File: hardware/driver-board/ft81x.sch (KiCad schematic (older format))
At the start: 4 parts, among them U4 FT813

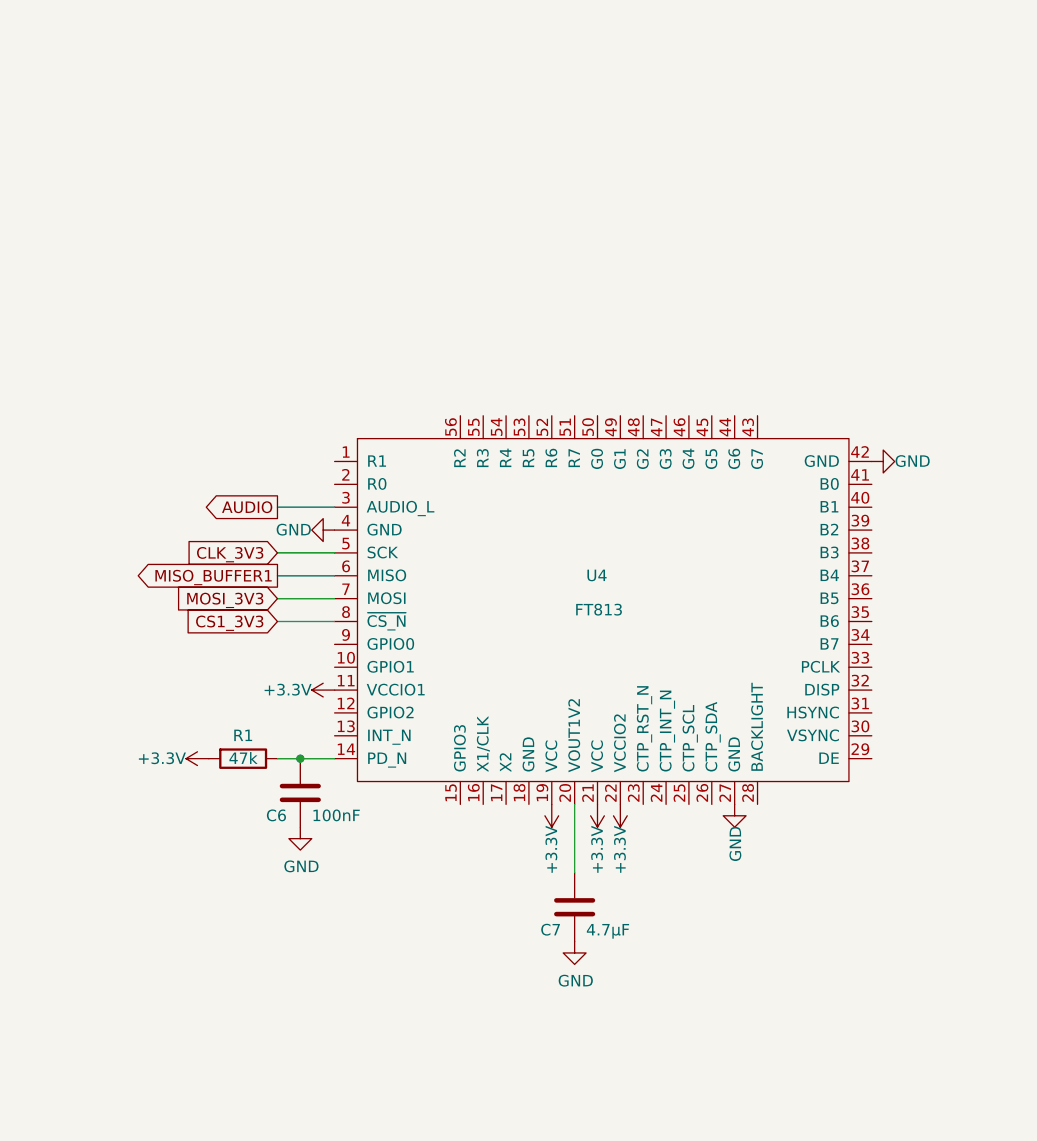
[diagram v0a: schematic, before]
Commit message: Rework power to four different voltage domains
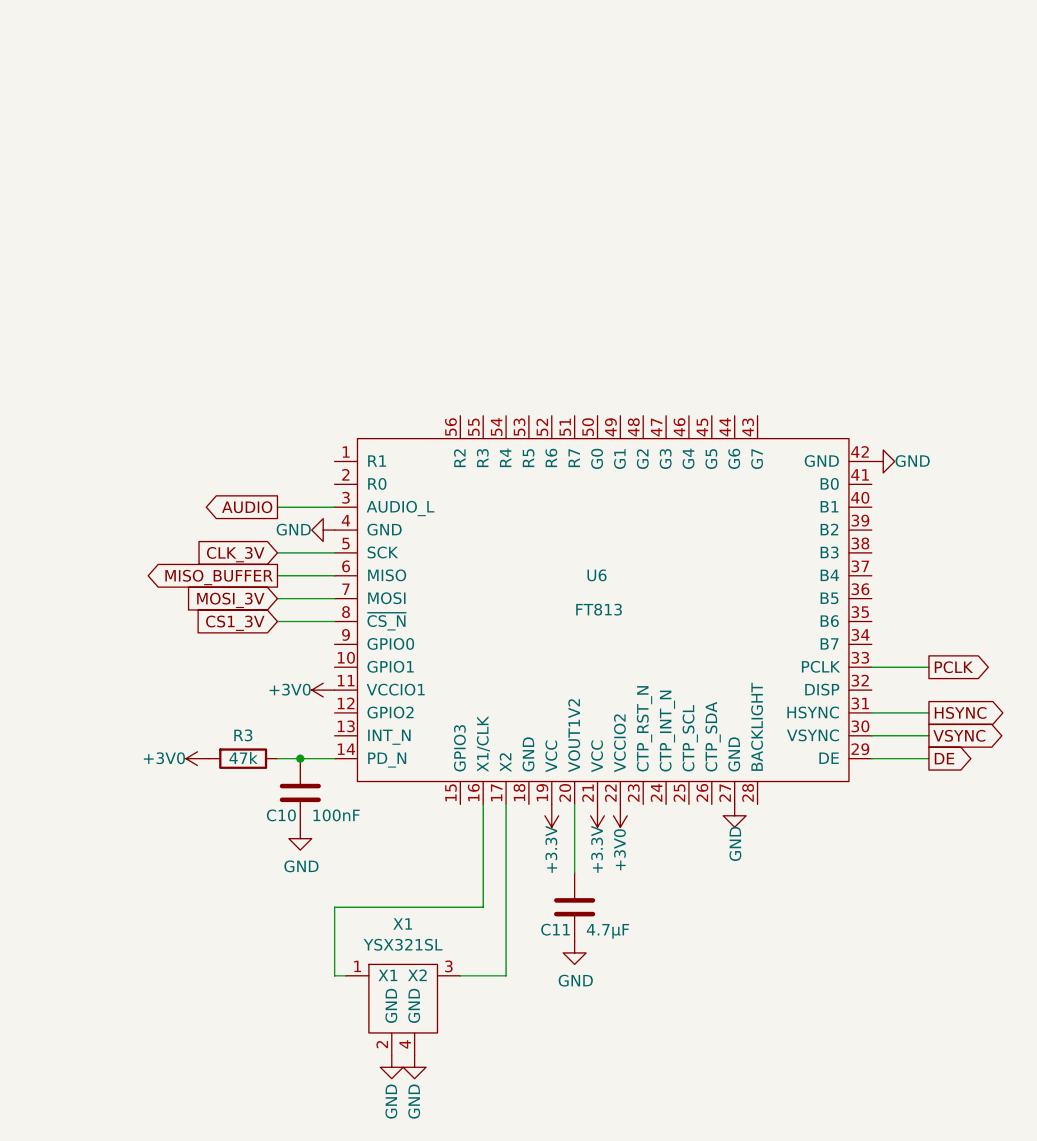
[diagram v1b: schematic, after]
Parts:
- added X1: YSX321SL, Crystal:Crystal_SMD_3225-4Pin_3.2x2.5mm, symbol driver-board:YSX321SL
- renumbered C6 to C10, C7 to C11, R1 to R3, U4 to U6
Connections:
- net +3V3: no longer R3.2, U6.11 (VCCIO1), U6.22 (VCCIO2)
- net GND: now also X1.2 (GND), X1.4 (GND)
- net at U6.16 (X1/CLK): now also X1.1 (X1)
- net at U6.17 (X2): now also X1.3 (X2)
- net DE: now reaches U6.29 (DE)
- net VSYNC: now reaches U6.30 (VSYNC)
- net HSYNC: now reaches U6.31 (HSYNC)
- net PCLK: now reaches U6.33 (PCLK)
- net CLK_3V3 renamed CLK_3V
- net CS1_3V3 renamed CS1_3V
- net MISO_BUFFER1 renamed MISO_BUFFER
- net MOSI_3V3 renamed MOSI_3V
- new net +3V0: R3.2, U6.11 (VCCIO1), U6.22 (VCCIO2)
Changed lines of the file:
@@
 $EndDescr
 $Comp
-L driver-board:FT813 U4
+L driver-board:FT813 U6
 U 1 1 5F0268C1
 P 5950 3750
-F 0 "U4" H 5900 3900 50  0000 L CNN
+F 0 "U6" H 5900 3900 50  0000 L CNN
 F 1 "FT813" H 5850 3750 50  0000 L CNN
 F 2 "Package_DFN_QFN:QFN-56-1EP_8x8mm_P0.5mm_EP5.6x5.6mm_HandSolder" H 5950 3750 50  0001 C CNN
@@
 AUDIO
 Text GLabel 4550 3500 0    50   Input ~ 0
-CLK_3V3
+CLK_3V
 Text GLabel 4550 3600 0    50   Output ~ 0
-MISO_BUFFER1
+MISO_BUFFER
 Text GLabel 4550 3700 0    50   Input ~ 0
-MOSI_3V3
+MOSI_3V
 Text GLabel 4550 3800 0    50   Input ~ 0
-CS1_3V3
-$Comp
-L power:GND #PWR021
+CS1_3V
+$Comp
+L power:GND #PWR034
 U 1 1 5F02B6C5
 P 4800 3400
-F 0 "#PWR021" H 4800 3150 50  0001 C CNN
+F 0 "#PWR034" H 4800 3150 50  0001 C CNN
 F 1 "GND" V 4800 3300 50  0000 R CNN
 F 2 "" H 4800 3400 50  0001 C CNN
@@
 $EndComp
 $Comp
-L power:+3.3V #PWR022
-U 1 1 5F02BA0F
-P 4800 4100
-F 0 "#PWR022" H 4800 3950 50  0001 C CNN
-F 1 "+3.3V" V 4800 4200 50  0000 L CNN
-F 2 "" H 4800 4100 50  0001 C CNN
-F 3 "" H 4800 4100 50  0001 C CNN
-	1    4800 4100
-	0    -1   -1   0
-$EndComp
-$Comp
-L power:+3.3V #PWR024
+L power:+3.3V #PWR037
 U 1 1 5F02BC5F
 P 5750 4600
-F 0 "#PWR024" H 5750 4450 50  0001 C CNN
+F 0 "#PWR037" H 5750 4450 50  0001 C CNN
 F 1 "+3.3V" V 5750 4800 50  0000 C CNN
 F 2 "" H 5750 4600 50  0001 C CNN
@@
 $EndComp
 $Comp
-L power:+3.3V #PWR025
+L power:+3.3V #PWR038
 U 1 1 5F02BEAA
 P 5950 4600
-F 0 "#PWR025" H 5950 4450 50  0001 C CNN
+F 0 "#PWR038" H 5950 4450 50  0001 C CNN
 F 1 "+3.3V" V 5950 4800 50  0000 C CNN
 F 2 "" H 5950 4600 50  0001 C CNN
@@
 $EndComp
 $Comp
-L power:+3.3V #PWR026
-U 1 1 5F02C0C1
-P 6050 4600
-F 0 "#PWR026" H 6050 4450 50  0001 C CNN
-F 1 "+3.3V" V 6050 4800 50  0000 C CNN
-F 2 "" H 6050 4600 50  0001 C CNN
-F 3 "" H 6050 4600 50  0001 C CNN
-	1    6050 4600
-	-1   0    0    1
-$EndComp
-$Comp
-L power:GND #PWR027
+L power:GND #PWR040
 U 1 1 5F02C6DE
 P 6550 4600
-F 0 "#PWR027" H 6550 4350 50  0001 C CNN
+F 0 "#PWR040" H 6550 4350 50  0001 C CNN
 F 1 "GND" V 6555 4427 50  0000 C CNN
 F 2 "" H 6550 4600 50  0001 C CNN
@@
 $EndComp
 $Comp
-L power:GND #PWR020
+L power:GND #PWR033
 U 1 1 5F02CB8C
 P 7150 3100
-F 0 "#PWR020" H 7150 2850 50  0001 C CNN
+F 0 "#PWR033" H 7150 2850 50  0001 C CNN
 F 1 "GND" V 7150 3000 50  0000 R CNN
 F 2 "" H 7150 3100 50  0001 C CNN
@@
 	4800 4400 4650 4400
 $Comp
-L Device:R R1
+L Device:R R3
 U 1 1 5F02D8F9
 P 4400 4400
-F 0 "R1" V 4300 4400 50  0000 C CNN
+F 0 "R3" V 4300 4400 50  0000 C CNN
 F 1 "47k" V 4400 4400 50  0000 C CNN
 F 2 "Resistor_SMD:R_0603_1608Metric" V 4330 4400 50  0001 C CNN
@@
 $EndComp
 $Comp
-L Device:C C6
+L Device:C C10
 U 1 1 5F02E8F5
 P 4650 4550
-F 0 "C6" H 4500 4450 50  0000 L CNN
+F 0 "C10" H 4500 4450 50  0000 L CNN
 F 1 "100nF" H 4700 4450 50  0000 L CNN
 F 2 "Capacitor_SMD:C_0603_1608Metric" H 4688 4400 50  0001 C CNN
@@
 	4650 4400 4550 4400
 $Comp
-L power:GND #PWR028
+L power:GND #PWR041
 U 1 1 5F02F445
 P 4650 4700
-F 0 "#PWR028" H 4650 4450 50  0001 C CNN
+F 0 "#PWR041" H 4650 4450 50  0001 C CNN
 F 1 "GND" H 4655 4527 50  0000 C CNN
 F 2 "" H 4650 4700 50  0001 C CNN
@@
 $EndComp
 $Comp
-L power:+3.3V #PWR023
-U 1 1 5F02F939
+L Device:C C11
+U 1 1 5F032943
+P 5850 5050
+F 0 "C11" H 5700 4950 50  0000 L CNN
+F 1 "4.7µF" H 5900 4950 50  0000 L CNN
+F 2 "Capacitor_SMD:C_0603_1608Metric" H 5888 4900 50  0001 C CNN
+F 3 "~" H 5850 5050 50  0001 C CNN
+	1    5850 5050
+	1    0    0    -1
+$EndComp
+Wire Wire Line
+	5850 4600 5850 4900
+$Comp
+L power:GND #PWR042
+U 1 1 5F033AAC
+P 5850 5200
+F 0 "#PWR042" H 5850 4950 50  0001 C CNN
+F 1 "GND" H 5855 5027 50  0000 C CNN
+F 2 "" H 5850 5200 50  0001 C CNN
+F 3 "" H 5850 5200 50  0001 C CNN
+	1    5850 5200
+	1    0    0    -1
+$EndComp
+Wire Wire Line
+	7150 4400 7400 4400
+Wire Wire Line
+	7150 4300 7400 4300
+Wire Wire Line
+	7150 4200 7400 4200
+Wire Wire Line
+	7150 4000 7400 4000
+Text GLabel 7400 4400 2    50   Output ~ 0
+DE
+Text GLabel 7400 4300 2    50   Output ~ 0
+VSYNC
+Text GLabel 7400 4200 2    50   Output ~ 0
+HSYNC
+Text GLabel 7400 4000 2    50   Output ~ 0
+PCLK
+$Comp
+L driver-board:YSX321SL X1
+U 1 1 5F0375EF
+P 5100 5400
+F 0 "X1" H 5100 5675 50  0000 C CNN
+F 1 "YSX321SL" H 5100 5584 50  0000 C CNN
+F 2 "Crystal:Crystal_SMD_3225-4Pin_3.2x2.5mm" H 5050 5400 50  0001 C CNN
+F 3 "" H 5050 5400 50  0001 C CNN
+	1    5100 5400
+	1    0    0    -1
+$EndComp
+$Comp
+L power:GND #PWR043
+U 1 1 5F03AD9F
+P 5050 5700
+F 0 "#PWR043" H 5050 5450 50  0001 C CNN
+F 1 "GND" V 5050 5500 50  0000 C CNN
+F 2 "" H 5050 5700 50  0001 C CNN
+F 3 "" H 5050 5700 50  0001 C CNN
+	1    5050 5700
+	1    0    0    -1
+$EndComp
+$Comp
+L power:GND #PWR044
+U 1 1 5F03AF97
+P 5150 5700
+F 0 "#PWR044" H 5150 5450 50  0001 C CNN
+F 1 "GND" V 5150 5500 50  0000 C CNN
+F 2 "" H 5150 5700 50  0001 C CNN
+F 3 "" H 5150 5700 50  0001 C CNN
+	1    5150 5700
+	1    0    0    -1
+$EndComp
+Wire Wire Line
+	5550 4600 5550 5350
+Wire Wire Line
+	5550 5350 5350 5350
+Wire Wire Line
+	5450 4600 5450 5050
+Wire Wire Line
+	5450 5050 4800 5050
+Wire Wire Line
+	4800 5050 4800 5350
+Wire Wire Line
+	4800 5350 4850 5350
+$Comp
+L power:+3V0 #PWR036
+U 1 1 5F0403D2
 P 4250 4400
-F 0 "#PWR023" H 4250 4250 50  0001 C CNN
-F 1 "+3.3V" V 4250 4500 50  0000 L CNN
+F 0 "#PWR036" H 4250 4250 50  0001 C CNN
+F 1 "+3V0" V 4250 4500 50  0000 L CNN
 F 2 "" H 4250 4400 50  0001 C CNN
 F 3 "" H 4250 4400 50  0001 C CNN
@@
 $EndComp
 $Comp
-L Device:C C7
-U 1 1 5F032943
-P 5850 5050
-F 0 "C7" H 5700 4950 50  0000 L CNN
-F 1 "4.7µF" H 5900 4950 50  0000 L CNN
-F 2 "Capacitor_SMD:C_0603_1608Metric" H 5888 4900 50  0001 C CNN
-F 3 "~" H 5850 5050 50  0001 C CNN
-	1    5850 5050
-	1    0    0    -1
-$EndComp
-Wire Wire Line
-	5850 4600 5850 4900
-$Comp
-L power:GND #PWR029
-U 1 1 5F033AAC
-P 5850 5200
-F 0 "#PWR029" H 5850 4950 50  0001 C CNN
-F 1 "GND" H 5855 5027 50  0000 C CNN
-F 2 "" H 5850 5200 50  0001 C CNN
-F 3 "" H 5850 5200 50  0001 C CNN
-	1    5850 5200
-	1    0    0    -1
+L power:+3V0 #PWR035
+U 1 1 5F040E18
+P 4800 4100
+F 0 "#PWR035" H 4800 3950 50  0001 C CNN
+F 1 "+3V0" V 4800 4200 50  0000 L CNN
+F 2 "" H 4800 4100 50  0001 C CNN
+F 3 "" H 4800 4100 50  0001 C CNN
+	1    4800 4100
+	0    -1   -1   0
+$EndComp
+$Comp
+L power:+3V0 #PWR039
+U 1 1 5F041F56
+P 6050 4600
+F 0 "#PWR039" H 6050 4450 50  0001 C CNN
+F 1 "+3V0" V 6050 4800 50  0000 C CNN
+F 2 "" H 6050 4600 50  0001 C CNN
+F 3 "" H 6050 4600 50  0001 C CNN
+	1    6050 4600
+	-1   0    0    1
 $EndComp
 $EndSCHEMATC

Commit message: Add display schematics
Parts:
- added C12: 10µF, Capacitor_SMD:C_0603_1608Metric, symbol Device:C
- added C13: 100nF, Capacitor_SMD:C_0603_1608Metric, symbol Device:C
- X1: JLCPCB (none) -> C9002
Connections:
- net +3V0: now also C13.1
- net +3V3: now also C12.1
- net GND: now also U6.18 (GND), C12.2, C13.2
- net B1: now reaches U6.1 (R1)
- net B0: now reaches U6.2 (R0)
- net R7: now reaches U6.34 (B7)
- net R6: now reaches U6.35 (B6)
- net R5: now reaches U6.36 (B5)
- net R4: now reaches U6.37 (B4)
- net R3: now reaches U6.38 (B3)
- net R2: now reaches U6.39 (B2)
- net R1: now reaches U6.40 (B1)
- net R0: now reaches U6.41 (B0)
- net G7: now reaches U6.43 (G7)
- net G6: now reaches U6.44 (G6)
- net G5: now reaches U6.45 (G5)
- net G4: now reaches U6.46 (G4)
- net G3: now reaches U6.47 (G3)
- net G2: now reaches U6.48 (G2)
- net G1: now reaches U6.49 (G1)
- net G0: now reaches U6.50 (G0)
- net B7: now reaches U6.51 (R7)
- net B6: now reaches U6.52 (R6)
- net B5: now reaches U6.53 (R5)
- net B4: now reaches U6.54 (R4)
- net B3: now reaches U6.55 (R3)
- net B2: now reaches U6.56 (R2)
- no-connect marks 0 -> 11
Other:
- moved on the sheet: C10, C11, R3, U6, X1

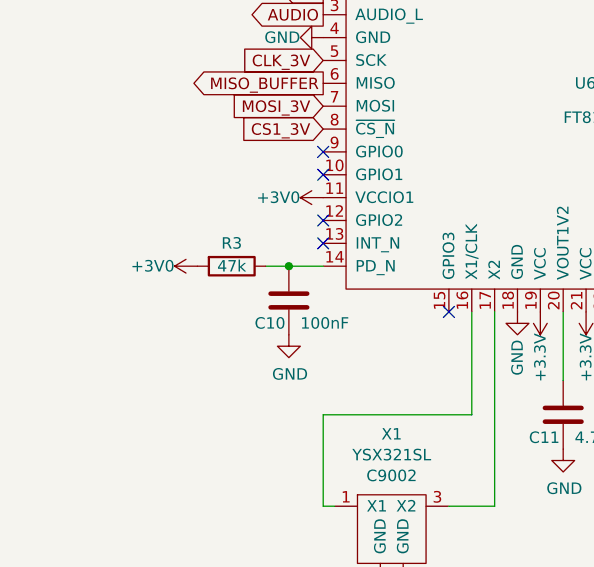
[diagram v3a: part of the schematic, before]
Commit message: Add more pin header pins
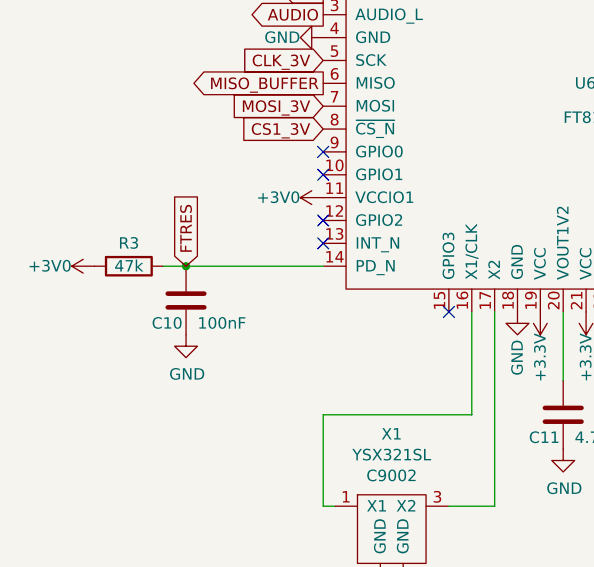
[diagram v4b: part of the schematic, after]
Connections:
- net FTRES: now reaches C10.1, R3.1, U6.14 (PD_N)
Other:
- moved on the sheet: C10, R3
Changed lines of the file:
@@
 $EndComp
 Wire Wire Line
-	4750 2900 4600 2900
+	4750 2900 4150 2900
 $Comp
 L Device:R R3
 U 1 1 5F02D8F9
-P 4350 2900
-F 0 "R3" V 4250 2900 50  0000 C CNN
-F 1 "47k" V 4350 2900 50  0000 C CNN
-F 2 "Resistor_SMD:R_0603_1608Metric" V 4280 2900 50  0001 C CNN
-F 3 "~" H 4350 2900 50  0001 C CNN
-	1    4350 2900
+P 3900 2900
+F 0 "R3" V 3800 2900 50  0000 C CNN
+F 1 "47k" V 3900 2900 50  0000 C CNN
+F 2 "Resistor_SMD:R_0603_1608Metric" V 3830 2900 50  0001 C CNN
+F 3 "~" H 3900 2900 50  0001 C CNN
+	1    3900 2900
 	0    1    1    0
 $EndComp
@@
 L Device:C C10
 U 1 1 5F02E8F5
-P 4600 3050
-F 0 "C10" H 4450 2950 50  0000 L CNN
-F 1 "100nF" H 4650 2950 50  0000 L CNN
-F 2 "Capacitor_SMD:C_0603_1608Metric" H 4638 2900 50  0001 C CNN
-F 3 "~" H 4600 3050 50  0001 C CNN
-	1    4600 3050
-	1    0    0    -1
-$EndComp
-Connection ~ 4600 2900
-Wire Wire Line
-	4600 2900 4500 2900
+P 4150 3050
+F 0 "C10" H 4000 2950 50  0000 L CNN
+F 1 "100nF" H 4200 2950 50  0000 L CNN
+F 2 "Capacitor_SMD:C_0603_1608Metric" H 4188 2900 50  0001 C CNN
+F 3 "~" H 4150 3050 50  0001 C CNN
+	1    4150 3050
+	1    0    0    -1
+$EndComp
+Connection ~ 4150 2900
+Wire Wire Line
+	4150 2900 4050 2900
 $Comp
 L power:GND #PWR042
 U 1 1 5F02F445
-P 4600 3200
-F 0 "#PWR042" H 4600 2950 50  0001 C CNN
-F 1 "GND" H 4605 3027 50  0000 C CNN
-F 2 "" H 4600 3200 50  0001 C CNN
-F 3 "" H 4600 3200 50  0001 C CNN
-	1    4600 3200
+P 4150 3200
+F 0 "#PWR042" H 4150 2950 50  0001 C CNN
+F 1 "GND" H 4155 3027 50  0000 C CNN
+F 2 "" H 4150 3200 50  0001 C CNN
+F 3 "" H 4150 3200 50  0001 C CNN
+	1    4150 3200
 	1    0    0    -1
 $EndComp
@@
 L power:+3V0 #PWR036
 U 1 1 5F0403D2
-P 4200 2900
-F 0 "#PWR036" H 4200 2750 50  0001 C CNN
-F 1 "+3V0" V 4200 3000 50  0000 L CNN
-F 2 "" H 4200 2900 50  0001 C CNN
-F 3 "" H 4200 2900 50  0001 C CNN
-	1    4200 2900
+P 3750 2900
+F 0 "#PWR036" H 3750 2750 50  0001 C CNN
+F 1 "+3V0" V 3750 3000 50  0000 L CNN
+F 2 "" H 3750 2900 50  0001 C CNN
+F 3 "" H 3750 2900 50  0001 C CNN
+	1    3750 2900
 	0    -1   -1   0
 $EndComp
@@
 	1    0    0    -1
 $EndComp
+Text GLabel 4150 2900 1    50   Input ~ 0
+FTRES
 $EndSCHEMATC

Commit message: Board layout on work
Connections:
- net IRQ: now reaches U6.13 (INT_N)
- no-connect marks 11 -> 10
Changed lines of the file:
@@
 NoConn ~ 7100 2600
 NoConn ~ 5300 3100
-NoConn ~ 4750 2800
 NoConn ~ 4750 2700
 NoConn ~ 4750 2500
@@
 Text GLabel 4150 2900 1    50   Input ~ 0
 FTRES
+Text GLabel 4750 2800 0    50   Output ~ 0
+IRQ
 $EndSCHEMATC

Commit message: Adapt new SPI signal names from OSHWA
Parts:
- U6: symbol driver-board:FT813 -> driver-board-rescue:FT813-driver-board-driver-board-rescue
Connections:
- net CLK_3V renamed SCK_3V
- net MISO_BUFFER renamed SDI_BUFFER
- net MOSI_3V renamed SDO_3V
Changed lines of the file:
@@
 $EndDescr
 $Comp
-L driver-board:FT813 U6
+L driver-board-rescue:FT813-driver-board-driver-board-rescue U6
 U 1 1 5F0268C1
 P 5900 2250
+AR Path="/5F0268C1" Ref="U6"  Part="1"
+AR Path="/5F022188/5F0268C1" Ref="U6"  Part="1"
 F 0 "U6" H 5850 2400 50  0000 L CNN
 F 1 "FT813" H 5800 2250 50  0000 L CNN
@@
 AUDIO
 Text GLabel 4750 2000 0    50   Input ~ 0
-CLK_3V
+SCK_3V
 Text GLabel 4750 2100 0    50   Output ~ 0
-MISO_BUFFER
+SDI_BUFFER
 Text GLabel 4750 2200 0    50   Input ~ 0
-MOSI_3V
+SDO_3V
 Text GLabel 4750 2300 0    50   Input ~ 0
 CS1_3V

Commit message: Add missing JLCPCB part numbers
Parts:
- C10, C13: JLCPCB (none) -> C14663
- C12: JLCPCB (none) -> C19702
- R3: JLCPCB (none) -> C23178
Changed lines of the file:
@@
 F 2 "Resistor_SMD:R_0603_1608Metric" V 3830 2900 50  0001 C CNN
 F 3 "~" H 3900 2900 50  0001 C CNN
+F 4 "C23178" H 3900 2900 50  0001 C CNN "JLCPCB"
 	1    3900 2900
 	0    1    1    0
@@
 F 2 "Capacitor_SMD:C_0603_1608Metric" H 4188 2900 50  0001 C CNN
 F 3 "~" H 4150 3050 50  0001 C CNN
+F 4 "C14663" H 4150 3050 50  0001 C CNN "JLCPCB"
 	1    4150 3050
 	1    0    0    -1
@@
 F 2 "Capacitor_SMD:C_0603_1608Metric" H 6388 4900 50  0001 C CNN
 F 3 "~" H 6350 5050 50  0001 C CNN
+F 4 "C19702" H 6350 5050 50  0001 C CNN "JLCPCB"
 	1    6350 5050
 	1    0    0    -1
@@
 F 2 "Capacitor_SMD:C_0603_1608Metric" H 7038 4900 50  0001 C CNN
 F 3 "~" H 7000 5050 50  0001 C CNN
+F 4 "C14663" H 7000 5050 50  0001 C CNN "JLCPCB"
 	1    7000 5050
 	1    0    0    -1

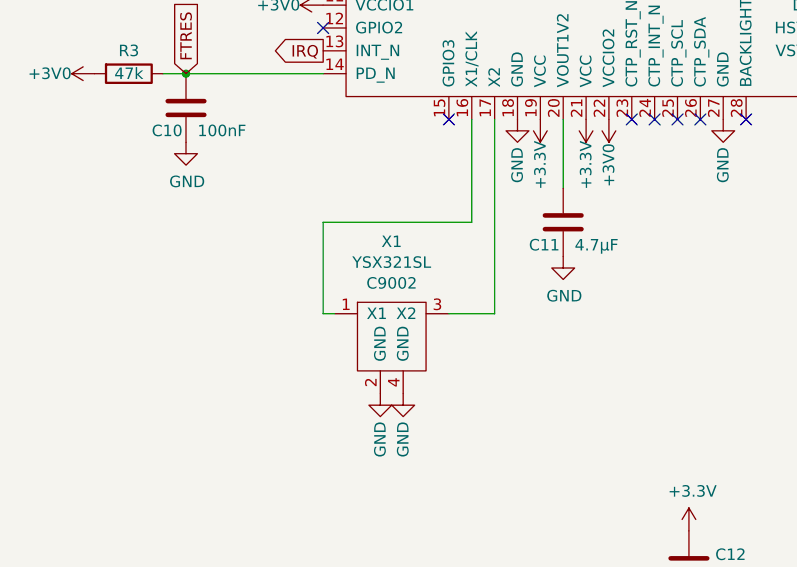
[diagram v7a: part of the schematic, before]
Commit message: Rename JLCPCB to LCSC and update PCB
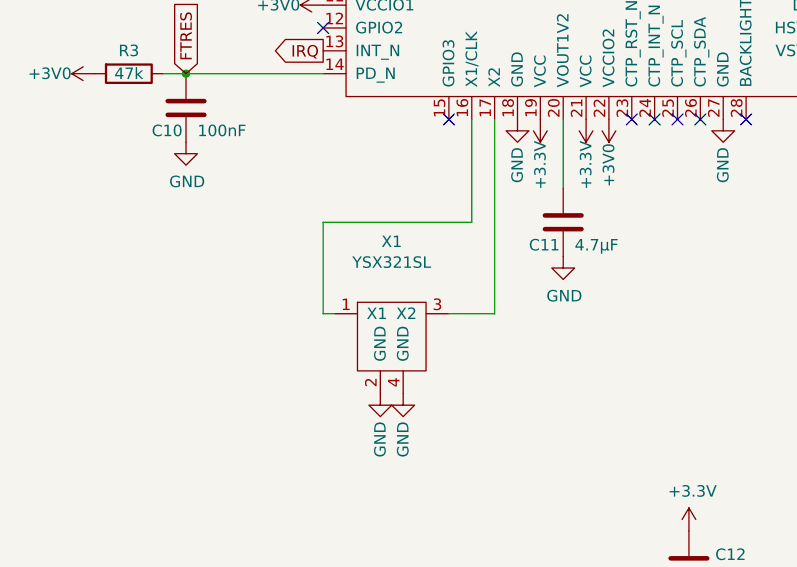
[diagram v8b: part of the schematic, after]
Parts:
- C10, C13: JLCPCB C14663 -> (none); LCSC (none) -> C14663
- C11: LCSC (none) -> C19666
- C12: JLCPCB C19702 -> (none); LCSC (none) -> C19702
- R3: JLCPCB C23178 -> (none); LCSC (none) -> C23178
- X1: JLCPCB C9002 -> (none); LCSC (none) -> C9002
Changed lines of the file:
@@
 F 2 "Resistor_SMD:R_0603_1608Metric" V 3830 2900 50  0001 C CNN
 F 3 "~" H 3900 2900 50  0001 C CNN
-F 4 "C23178" H 3900 2900 50  0001 C CNN "JLCPCB"
+F 4 "C23178" H 3900 2900 50  0001 C CNN "LCSC"
 	1    3900 2900
 	0    1    1    0
@@
 F 2 "Capacitor_SMD:C_0603_1608Metric" H 4188 2900 50  0001 C CNN
 F 3 "~" H 4150 3050 50  0001 C CNN
-F 4 "C14663" H 4150 3050 50  0001 C CNN "JLCPCB"
+F 4 "C14663" H 4150 3050 50  0001 C CNN "LCSC"
 	1    4150 3050
 	1    0    0    -1
@@
 F 2 "Capacitor_SMD:C_0603_1608Metric" H 5838 3400 50  0001 C CNN
 F 3 "~" H 5800 3550 50  0001 C CNN
+F 4 "C19666" H 5800 3550 50  0001 C CNN "LCSC"
 	1    5800 3550
 	1    0    0    -1
@@
 F 2 "Crystal:Crystal_SMD_3225-4Pin_3.2x2.5mm" H 5000 4000 50  0001 C CNN
 F 3 "" H 5000 4000 50  0001 C CNN
-F 4 "C9002" H 5050 4183 50  0000 C CNN "JLCPCB"
+F 4 "C9002" H 5050 4000 50  0001 C CNN "LCSC"
 	1    5050 4000
 	1    0    0    -1
@@
 F 2 "Capacitor_SMD:C_0603_1608Metric" H 6388 4900 50  0001 C CNN
 F 3 "~" H 6350 5050 50  0001 C CNN
-F 4 "C19702" H 6350 5050 50  0001 C CNN "JLCPCB"
+F 4 "C19702" H 6350 5050 50  0001 C CNN "LCSC"
 	1    6350 5050
 	1    0    0    -1
@@
 F 2 "Capacitor_SMD:C_0603_1608Metric" H 7038 4900 50  0001 C CNN
 F 3 "~" H 7000 5050 50  0001 C CNN
-F 4 "C14663" H 7000 5050 50  0001 C CNN "JLCPCB"
+F 4 "C14663" H 7000 5050 50  0001 C CNN "LCSC"
 	1    7000 5050
 	1    0    0    -1
